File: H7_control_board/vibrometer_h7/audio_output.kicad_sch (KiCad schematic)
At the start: 31 parts, among them J901 PJ-3270, U901 RC4580, U902 TPA6111A2

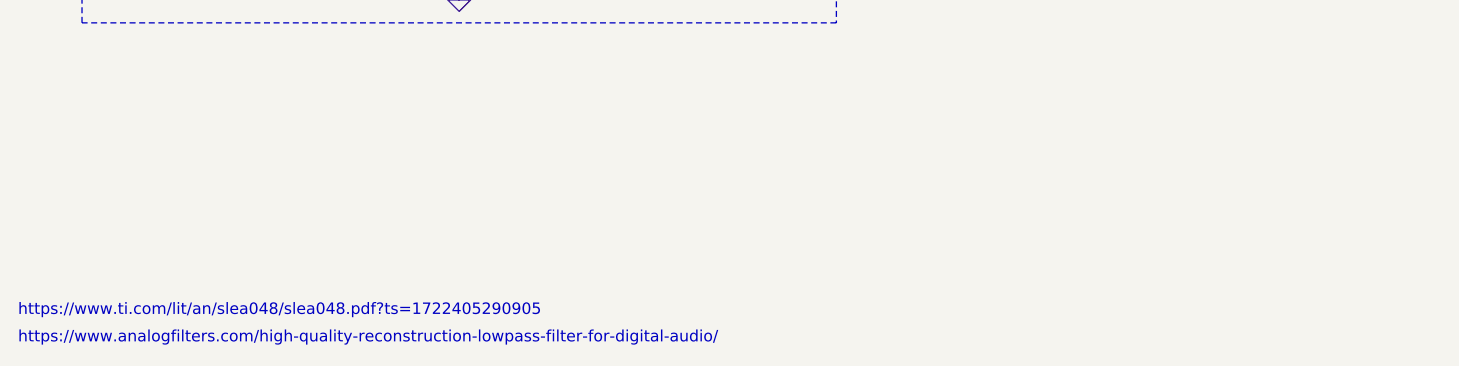
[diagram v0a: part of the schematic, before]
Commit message: worked on power supply filtering
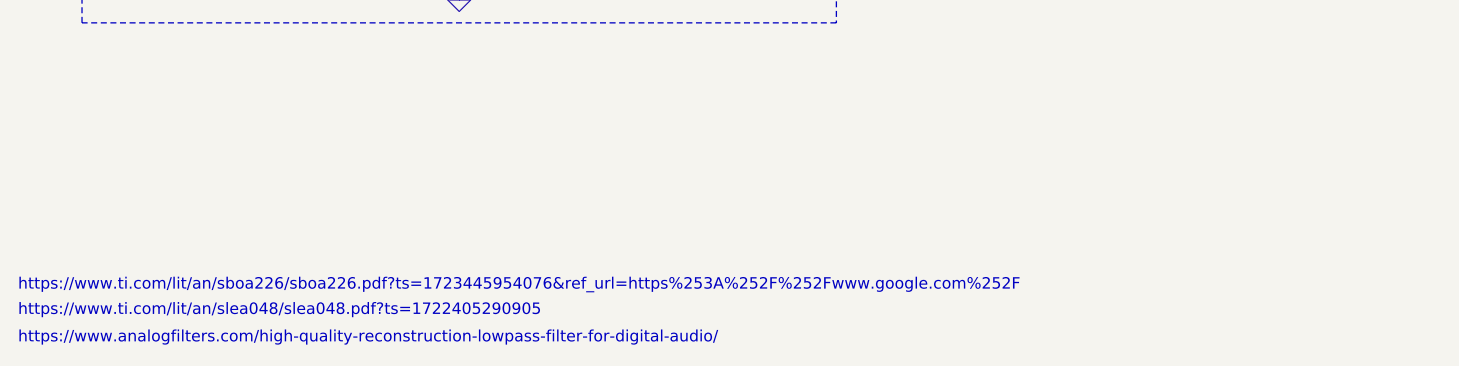
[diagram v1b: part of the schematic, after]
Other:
- note added: "https://www.ti.com/lit/an/sboa226/sboa226.pdf?ts=1723445954076&ref_url=https%253A%252F%252Fwww.google.com%252F"
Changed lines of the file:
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@@
+		)
+	)
+	(text "https://www.ti.com/lit/an/sboa226/sboa226.pdf?ts=1723445954076&ref_url=https%253A%252F%252Fwww.google.com%252F"
+		(exclude_from_sim no)
+		(at 17.018 188.468 0)
+		(effects
+			(font
+				(size 1.27 1.27)
+			)
+			(justify left top)
 		)
 	)

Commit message: first pass at board routing
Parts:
- C901, C909: footprint Capacitor_SMD:C_0603_1608Metric -> Capacitor_SMD:C_0402_1005Metric_Pad0.74x0.62mm_HandSolder
- C904, C905: footprint Capacitor_SMD:C_0603_1608Metric -> (none)
- C911, C912, C913, C914, C915, C916: LCSC C45783 -> C15850
- U901: footprint (none) -> Package_SO:SOIC-8-1EP_3.9x4.9mm_P1.27mm_EP2.41x3.81mm; LCSC (none) -> C80100
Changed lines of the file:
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@@
 			)
 		)
-		(property "Footprint" "Capacitor_SMD:C_0603_1608Metric"
+		(property "Footprint" "Capacitor_SMD:C_0402_1005Metric_Pad0.74x0.62mm_HandSolder"
 			(at 39.37 34.29 0)
 			(effects
@@
 			)
 		)
-		(property "Datasheet" "https://wmsc.lcsc.com/wmsc/upload/file/pdf/v2/lcsc/2304140030_Samsung-Electro-Mechanics-CL21A226MAQNNNE_C45783.pdf"
+		(property "Datasheet" "CL21A106KAYNNNE_C15850.pdf"
 			(at 228.6 104.14 0)
 			(effects
@@
 			)
 		)
-		(property "LCSC" "C45783"
+		(property "LCSC" "C15850"
 			(at 228.6 104.14 0)
 			(effects
@@
 			)
 		)
-		(property "Footprint" ""
+		(property "Footprint" "Package_SO:SOIC-8-1EP_3.9x4.9mm_P1.27mm_EP2.41x3.81mm"
 			(at 83.82 83.82 0)
 			(effects
@@
 			)
 		)
+		(property "LCSC" "C80100"
+			(at 83.82 83.82 0)
+			(effects
+				(font
+					(size 1.27 1.27)
+				)
+				(hide yes)
+			)
+		)
 		(pin "2"
 		)
@@
 			)
 		)
-		(property "Footprint" "Capacitor_SMD:C_0603_1608Metric"
+		(property "Footprint" ""
 			(at 77.47 119.38 0)
 			(effects
@@
 			)
 		)
-		(property "Datasheet" "https://wmsc.lcsc.com/wmsc/upload/file/pdf/v2/lcsc/2304140030_Samsung-Electro-Mechanics-CL21A226MAQNNNE_C45783.pdf"
+		(property "Datasheet" "CL21A106KAYNNNE_C15850.pdf"
 			(at 228.6 96.52 0)
 			(effects
@@
 			)
 		)
-		(property "LCSC" "C45783"
+		(property "LCSC" "C15850"
 			(at 228.6 96.52 0)
 			(effects
@@
 			)
 		)
-		(property "Datasheet" "https://wmsc.lcsc.com/wmsc/upload/file/pdf/v2/lcsc/2304140030_Samsung-Electro-Mechanics-CL21A226MAQNNNE_C45783.pdf"
+		(property "Datasheet" "CL21A106KAYNNNE_C15850.pdf"
 			(at 228.6 115.57 0)
 			(effects
@@
 			)
 		)
-		(property "LCSC" "C45783"
+		(property "LCSC" "C15850"
 			(at 228.6 115.57 0)
 			(effects
@@
 			)
 		)
-		(property "Datasheet" "https://wmsc.lcsc.com/wmsc/upload/file/pdf/v2/lcsc/2304140030_Samsung-Electro-Mechanics-CL21A226MAQNNNE_C45783.pdf"
+		(property "Datasheet" "CL21A106KAYNNNE_C15850.pdf"
 			(at 228.6 119.38 0)
 			(effects
@@
 			)
 		)
-		(property "LCSC" "C45783"
+		(property "LCSC" "C15850"
 			(at 228.6 119.38 0)
 			(effects
@@
 			)
 		)
-		(property "Datasheet" "https://wmsc.lcsc.com/wmsc/upload/file/pdf/v2/lcsc/2304140030_Samsung-Electro-Mechanics-CL21A226MAQNNNE_C45783.pdf"
+		(property "Datasheet" "CL21A106KAYNNNE_C15850.pdf"
 			(at 228.6 100.33 0)
 			(effects
@@
 			)
 		)
-		(property "LCSC" "C45783"
+		(property "LCSC" "C15850"
 			(at 228.6 100.33 0)
 			(effects
@@
 			)
 		)
-		(property "Footprint" "Capacitor_SMD:C_0603_1608Metric"
+		(property "Footprint" ""
 			(at 77.47 69.85 0)
 			(effects
@@
 			)
 		)
-		(property "Footprint" ""
+		(property "Footprint" "Package_SO:SOIC-8-1EP_3.9x4.9mm_P1.27mm_EP2.41x3.81mm"
 			(at 48.26 38.1 0)
 			(effects
@@
 		)
 		(property "Description" "Dual Audio Operational Amplifier, SOIC-8/SSOP-8"
+			(at 48.26 38.1 0)
+			(effects
+				(font
+					(size 1.27 1.27)
+				)
+				(hide yes)
+			)
+		)
+		(property "LCSC" "C80100"
 			(at 48.26 38.1 0)
 			(effects
@@
 			)
 		)
-		(property "Footprint" ""
+		(property "Footprint" "Package_SO:SOIC-8-1EP_3.9x4.9mm_P1.27mm_EP2.41x3.81mm"
 			(at 83.82 134.62 0)
 			(effects
@@
 			)
 		)
+		(property "LCSC" "C80100"
+			(at 83.82 134.62 0)
+			(effects
+				(font
+					(size 1.27 1.27)
+				)
+				(hide yes)
+			)
+		)
 		(pin "2"
 		)
@@
 			)
 		)
-		(property "Footprint" "Capacitor_SMD:C_0603_1608Metric"
+		(property "Footprint" "Capacitor_SMD:C_0402_1005Metric_Pad0.74x0.62mm_HandSolder"
 			(at 186.69 95.25 0)
 			(effects
@@
 			)
 		)
-		(property "Datasheet" "https://wmsc.lcsc.com/wmsc/upload/file/pdf/v2/lcsc/2304140030_Samsung-Electro-Mechanics-CL21A226MAQNNNE_C45783.pdf"
+		(property "Datasheet" "CL21A106KAYNNNE_C15850.pdf"
 			(at 228.6 123.19 0)
 			(effects
@@
 			)
 		)
-		(property "LCSC" "C45783"
+		(property "LCSC" "C15850"
 			(at 228.6 123.19 0)
 			(effects

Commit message: lots of routing progress!!
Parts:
- renumbered R_b901 to R905, R905 to R906, R_a901 to R907, R906 to R908, R907 to R909, R908 to R910, R909 to R911
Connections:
- net AMP1_FB: now reaches R904.2, R906.1, U901.2 (-)
- net LN_OUT1: now reaches C911.1, C912.1, C913.1, R910.2, U902.7 (VO1)
- net AUDIO_R: now reaches C911.2, C912.2, C913.2, J901.R
- net AMP1_OUT: now reaches C904.1, C906.1, R906.2, U901.1
- net AMP1_IN: now reaches C902.2, R903.2, U901.3 (+)
- net AMP2_OUT: now reaches C905.1, C907.1, R907.2, U901.7
- net AMP2_FILT: now reaches C905.2, R902.2, R_in901.1
- net AUDIO_L: now reaches C914.2, C915.2, C916.2, J901.T
- net LN_IN1: now reaches R908.2, R910.1, U902.8 (IN1-)
- net LN_IN2: now reaches R909.2, R911.1, U902.4 (IN2-)
- net LN_OUT2: now reaches C914.1, C915.1, C916.1, R911.2, U902.5 (VO2)
- net AMP2_IN: now reaches C903.2, R_in901.2, U901.5 (+)
- net AMP1_FILT: now reaches C904.2, R901.2, R903.1
- net LN_BYPASS: now reaches C910.2, U902.1 (BYPASS)
- net AMP2_FB: now reaches R905.2, R907.1, U901.6 (-)
- net +5V renamed +5VA

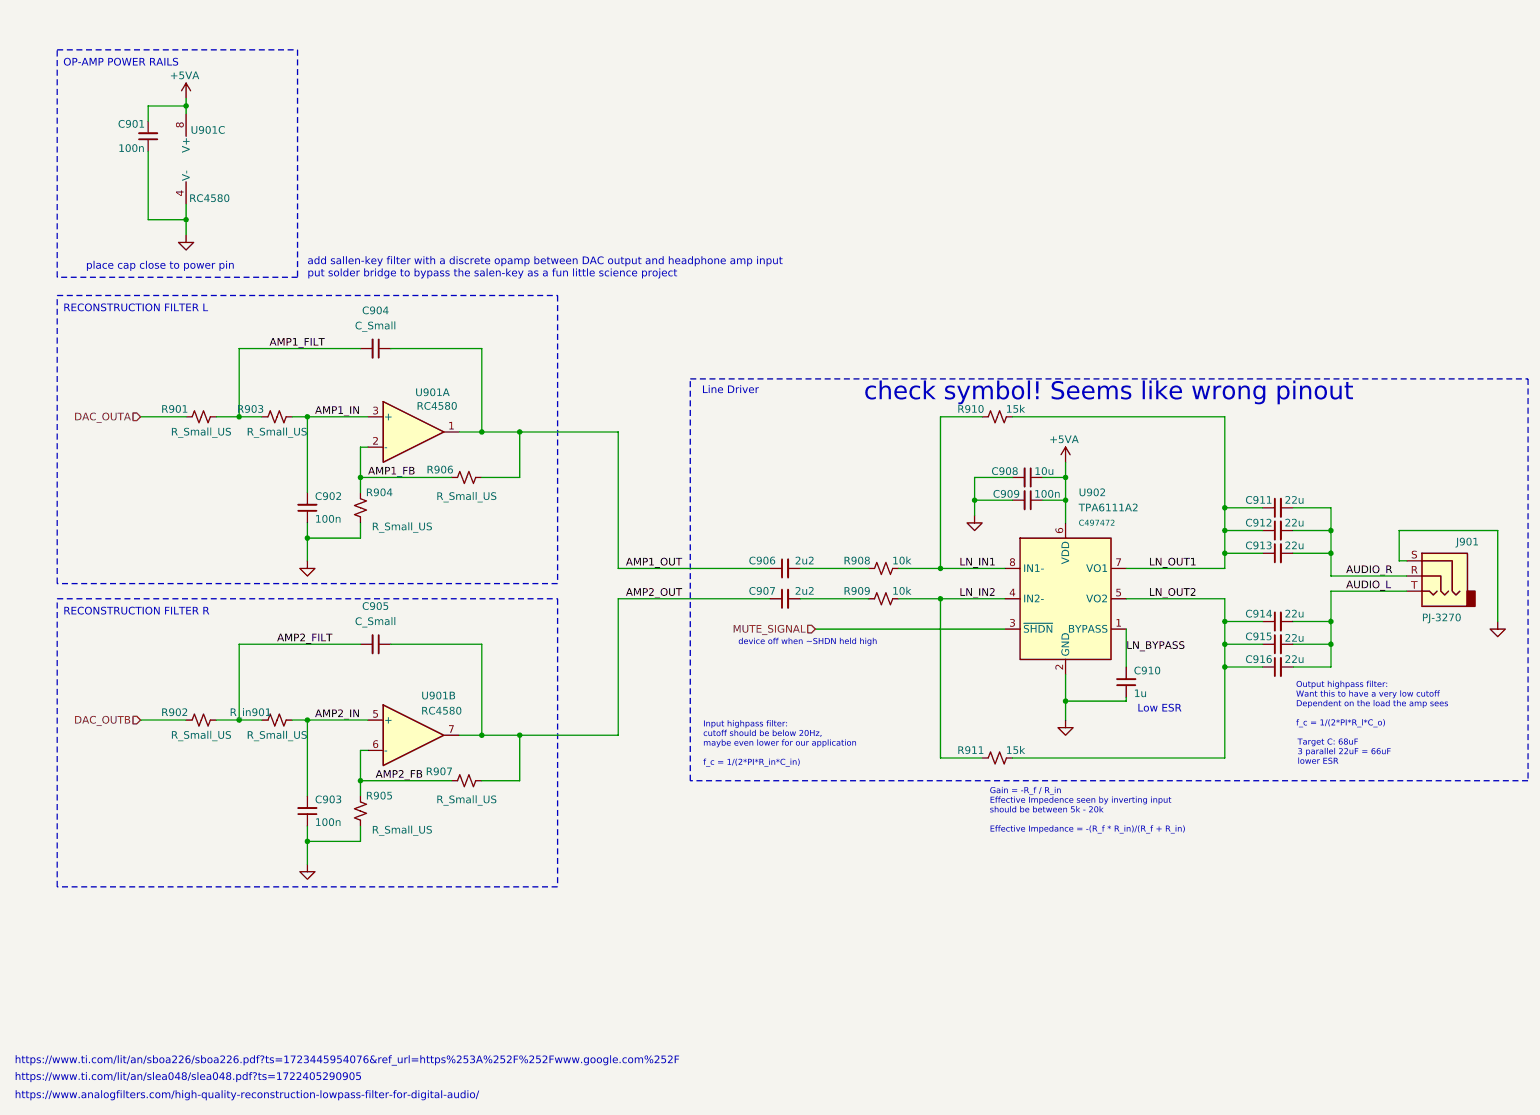
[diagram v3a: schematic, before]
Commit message: zero unrouts! But still need to fix footprint for headphone jack. So 3 unrouts!
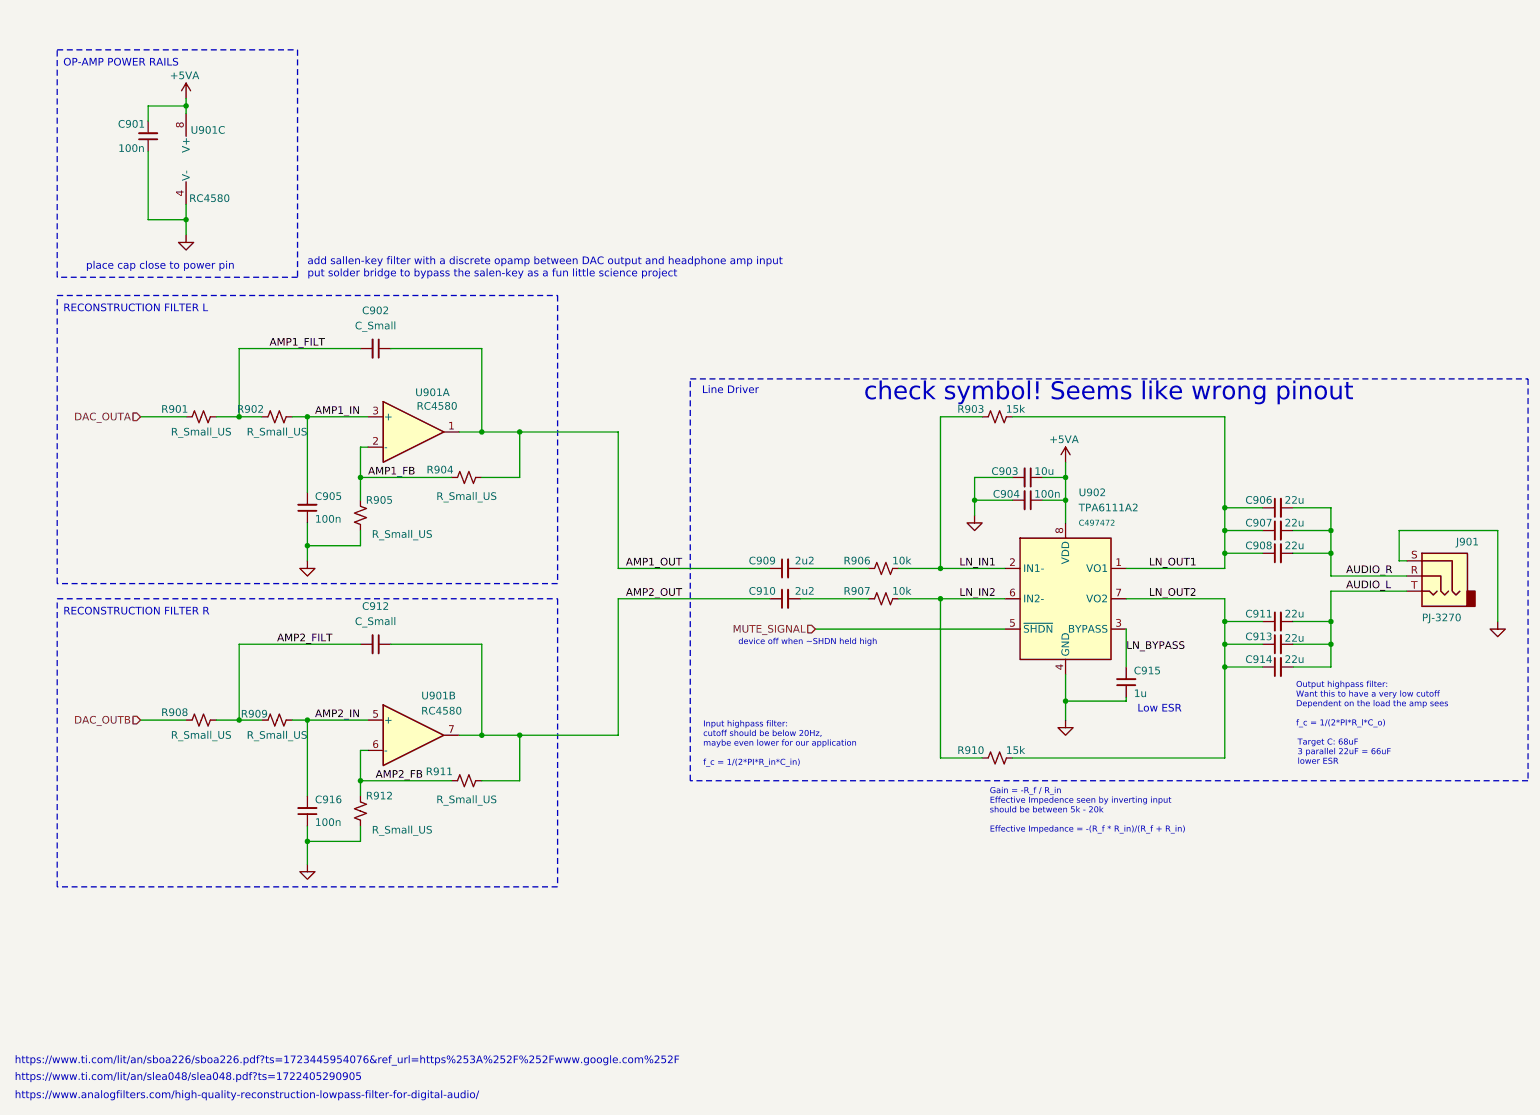
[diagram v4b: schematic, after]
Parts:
- C902: renamed from C904; footprint (none) -> Capacitor_SMD:C_0603_1608Metric
- C912: renamed from C905; footprint (none) -> Capacitor_SMD:C_0603_1608Metric
- C915: renamed from C910; footprint Capacitor_SMD:C_0805_2012Metric -> Capacitor_SMD:C_0603_1608Metric; LCSC C28323 -> C15849
- R901: footprint (none) -> Resistor_SMD:R_0603_1608Metric
- R902: renamed from R903; footprint (none) -> Resistor_SMD:R_0603_1608Metric
- R904: renamed from R906; footprint (none) -> Resistor_SMD:R_0603_1608Metric
- R905: renamed from R904; footprint (none) -> Resistor_SMD:R_0603_1608Metric
- R906: renamed from R908; footprint Resistor_SMD:R_0805_2012Metric -> Resistor_SMD:R_0603_1608Metric; LCSC C17414 -> C25744
- R907: renamed from R909; footprint Resistor_SMD:R_0805_2012Metric -> Resistor_SMD:R_0603_1608Metric; LCSC C17414 -> C25744
- R908: renamed from R902; footprint (none) -> Resistor_SMD:R_0603_1608Metric
- R909: renamed from R_in901; footprint (none) -> Resistor_SMD:R_0603_1608Metric
- R911: renamed from R907; footprint (none) -> Resistor_SMD:R_0603_1608Metric
- R912: renamed from R905; footprint (none) -> Resistor_SMD:R_0603_1608Metric
- renumbered C908 to C903, C909 to C904, C902 to C905, C911 to C906, C912 to C907, C913 to C908, C906 to C909, C907 to C910, C914 to C911, C915 to C913, C916 to C914, C903 to C916, R910 to R903, R911 to R910
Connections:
- net +5VA: now also U902.8 (VDD); no longer U902.6 (VDD)
- net GND: now also U902.4 (GND); no longer U902.2 (GND)
- net LN_BYPASS: now also U902.3 (BYPASS); no longer U902.1 (BYPASS)
- net LN_IN1: now also U902.2 (IN1-); no longer U902.8 (IN1-)
- net LN_IN2: now also U902.6 (IN2-); no longer U902.4 (IN2-)
- net LN_OUT1: now also U902.1 (VO1); no longer U902.7 (VO1)
- net LN_OUT2: now also U902.7 (VO2); no longer U902.5 (VO2)
- net MUTE_SIGNAL: now also U902.5 (~{SHDN}); no longer U902.3 (~{SHDN})
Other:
- moved on the sheet: R905
